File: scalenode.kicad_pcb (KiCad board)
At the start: 4 copper layers, 173.5 x 40 mm, 161 parts, among them IC2 TPS2378DDA, J1 QSE-020-01-F-D, J2 QSE-020-01-F-D, J3 1-2199230-6, J4 1140084168, J5 0473460001, J6 SS-74800-144, J7 DF40HC(3.0)-100DS-0.4v, J8 DF40HC(3.0)-100DS-0.4v, M1 compute-module-4-1.5mm, Q1 MMBT3906,215, Q2 MMBT3906,215, Q3 SI7848BDP-T1-E3, Q4 SI7450DP-T1-GE3, Q5 MMBT3906,215, T1 P0926NL, T2 POE300F-50L, U1 TS3USB30EDGSR, U2 TPS62823DLCT, U3 UCC3809D2, U4 TCMT1107

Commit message: Update designators
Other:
- board text added: "Expansion"
- board text added: "Video"
- board text removed: "Adapter Connector"
- board text removed: "Debug Connector"

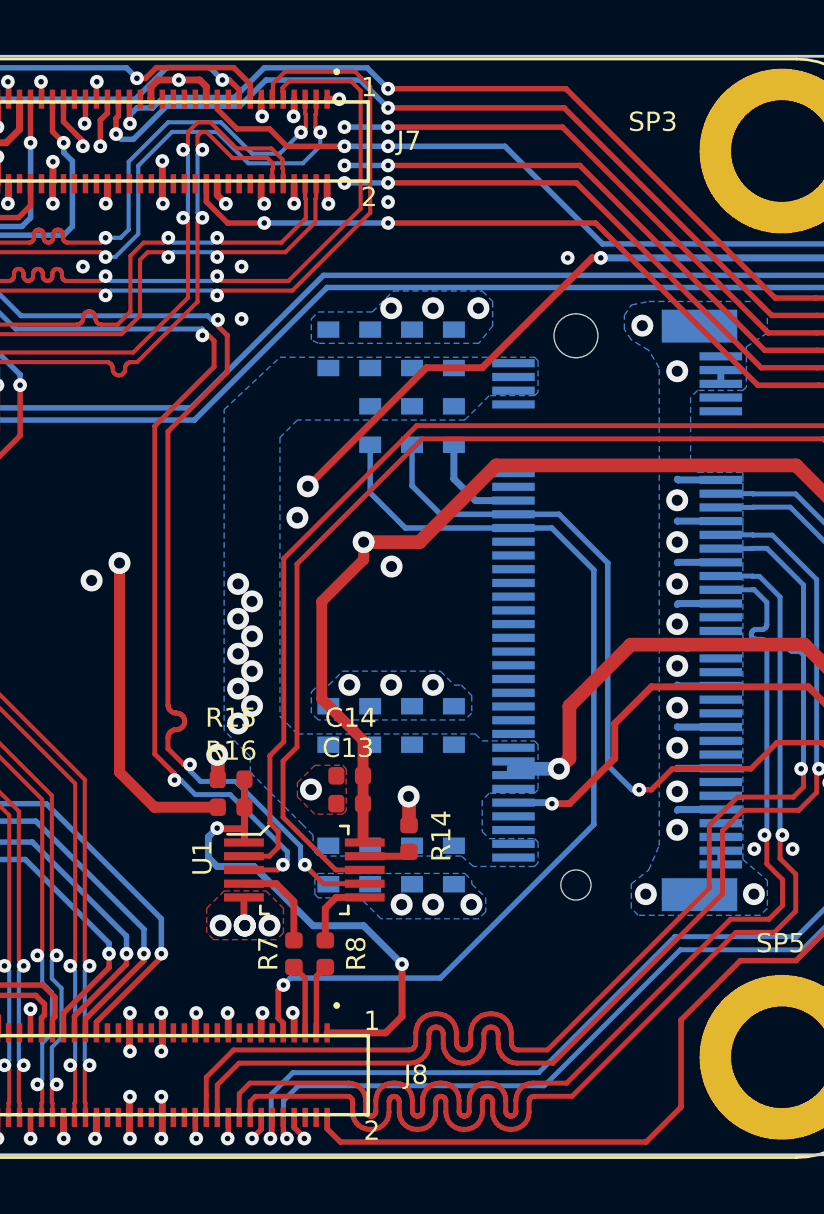
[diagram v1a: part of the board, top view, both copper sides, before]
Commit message: Fix J7 J8 footprints
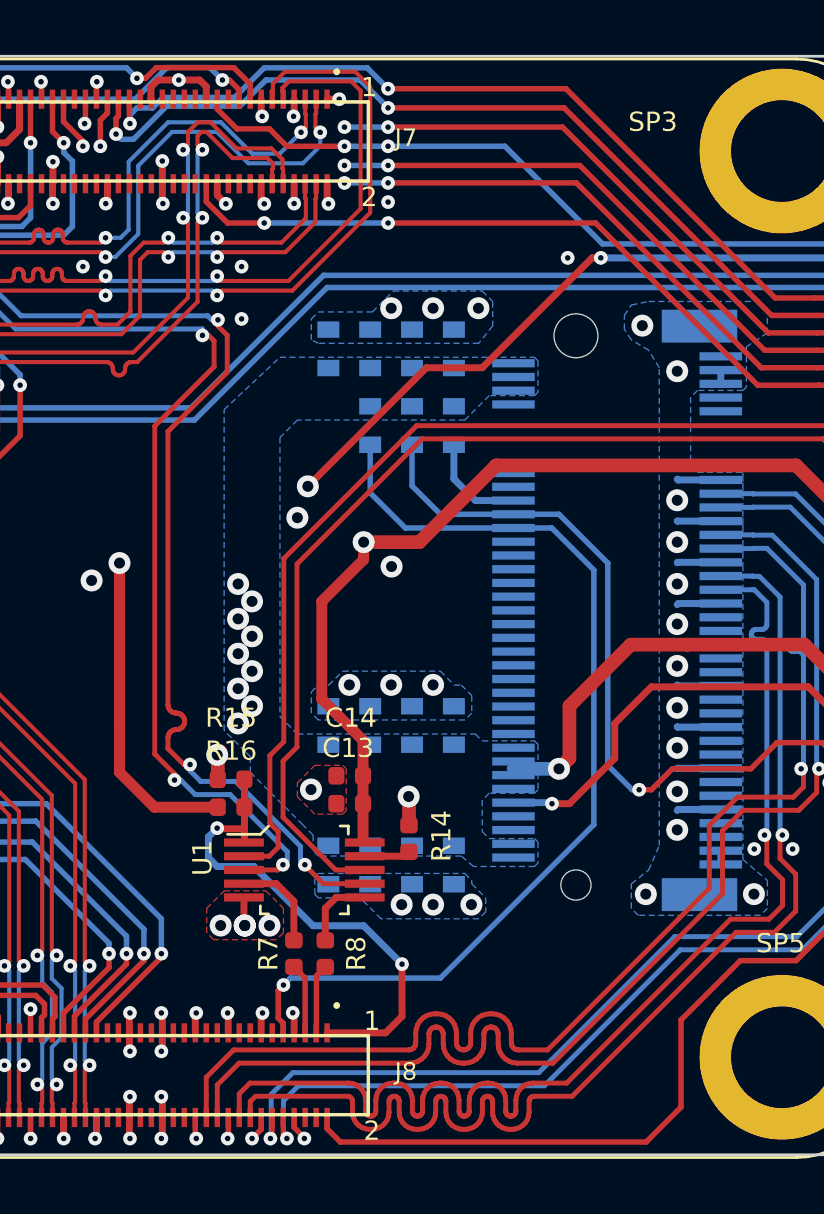
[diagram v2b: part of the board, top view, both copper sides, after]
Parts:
- J7, J8: footprint antmicro-footprints:DF40HC(3.0)-100DS-0.4v -> scalenode-footprints:DF40HC-3.0-100DS-0.4v

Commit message: Fix logotype
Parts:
- N1: footprint antmicro-footprints:antmicro-logo_scaled_15mm -> scalenode-footprints:antmicro-logo_scaled_15mm

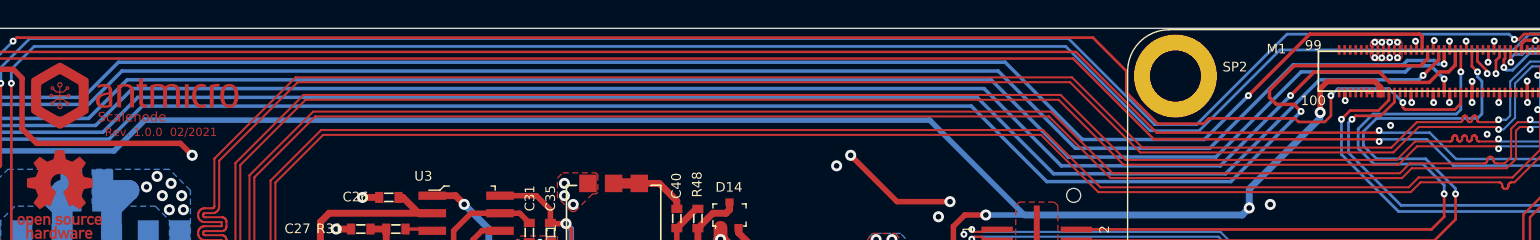
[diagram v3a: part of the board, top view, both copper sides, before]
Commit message: Connect GPIO_VREF signal to 3.3V_RPi
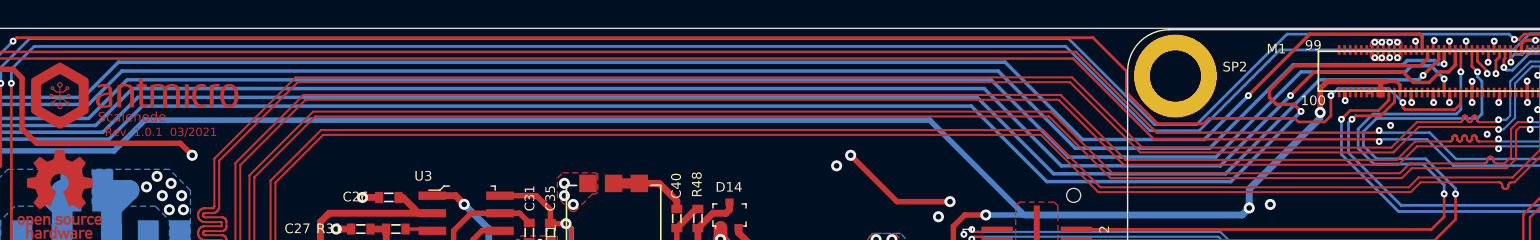
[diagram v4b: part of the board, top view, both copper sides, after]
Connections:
- J7 pad 78: GPIO_VREF -> 3V3_RPi
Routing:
- net 3V3_RPi: track 274.7 -> 277.0 mm
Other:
- board text added: "Rev. 1.0.1 03/2021"

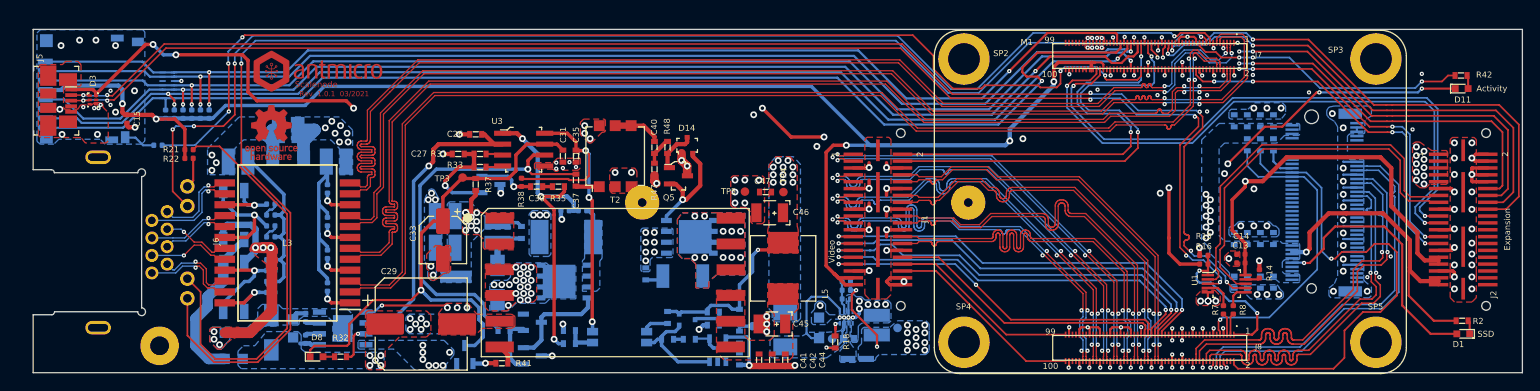
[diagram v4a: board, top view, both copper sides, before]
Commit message: Migration to KiCad 6
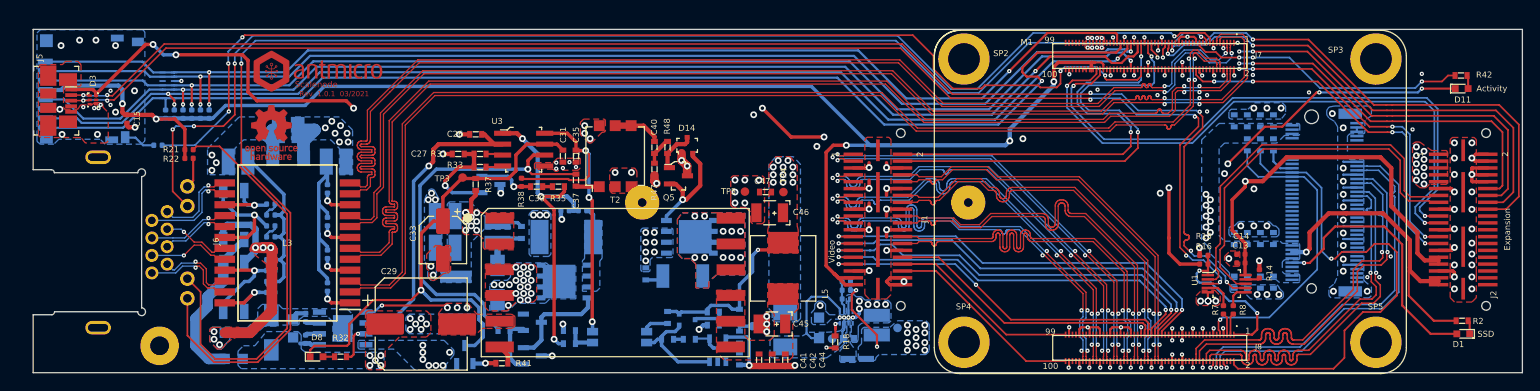
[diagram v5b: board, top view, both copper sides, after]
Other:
- outline, holes or cut-outs redrawn
- net class Default removed
- net class Diff_100 removed
- net class Diff_90 removed

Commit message: Implemented changes from rev 1.0.4. New components initial placement
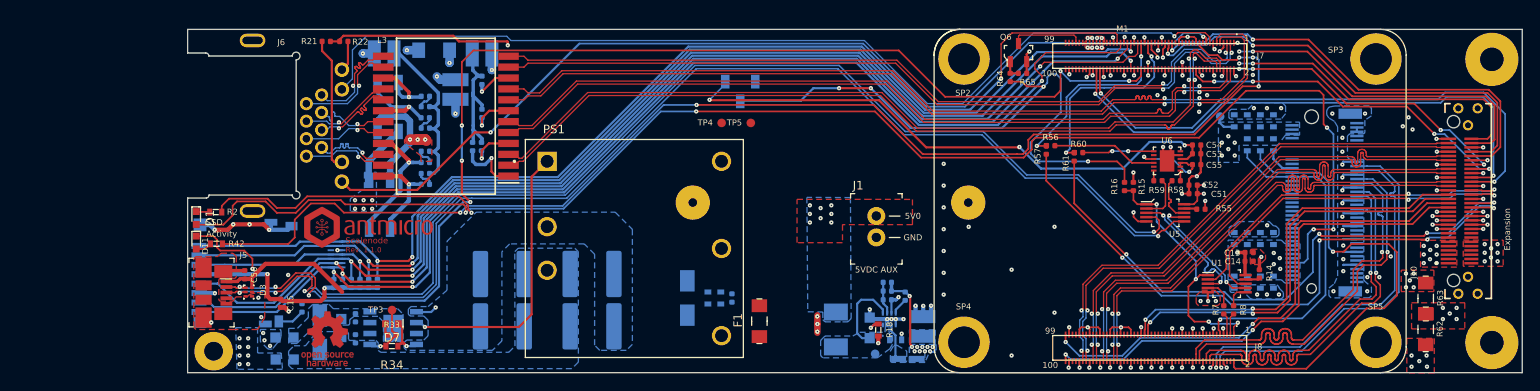
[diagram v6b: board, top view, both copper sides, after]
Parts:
- removed C21, C23, C24: C_10n_0402, scalenode-footprints:0402-cap
- removed C22: C_1n_1210_2kV, scalenode-footprints:1210-cap
- removed C38: C_100p_0402, scalenode-footprints:0402-cap
- removed C39: C_82n_0603, scalenode-footprints:0603-cap
- removed C40: C_470n_0603, scalenode-footprints:0603-cap
- removed C41, C42, C44: C_47u_0603, scalenode-footprints:0603-cap
- removed C43, C47: C_1u_0603, scalenode-footprints:0603-cap
- removed C45, C46: C_220u_KEMET_B, scalenode-footprints:KEMET_B
- removed C48: C_1n_0603, scalenode-footprints:0603-cap
- removed C49: C_1n2_0603, scalenode-footprints:0603-res
- removed D10: MURA120T3G, scalenode-footprints:DO-214AC
- removed D12: TLV431ACDBVR, scalenode-footprints:SOT-23-5
- removed D13, D14: BAV99W,115, scalenode-footprints:SOT-323
- removed D9: BAS16E6327HTSA1, scalenode-footprints:SOT-23-3
- removed IC2: TPS2378DDA, scalenode-footprints:SOIC127P600X170-9N
- removed J2: QSE-020-01-F-D, scalenode-footprints:QSE-020-01-XXX-D-A
- removed L4: DO1608C-332MLB, scalenode-footprints:L_6.3x4.5
- removed L5: DR74-R33-R, scalenode-footprints:L_DR74
- removed Q1, Q2, Q5: MMBT3906,215, scalenode-footprints:SOT-23-3
- removed Q3: SI7848BDP-T1-E3, scalenode-footprints:PowerPAK_SO-8_Single
- removed Q4: SI7450DP-T1-GE3, scalenode-footprints:PowerPAK_SO-8_Single
- removed R36: R_24k9_0402, scalenode-footprints:0402-res
- removed R37: R_30k1_0603, scalenode-footprints:0603-res
- removed R38: R_4k99_0402, scalenode-footprints:0402-res
- removed R39: R_24R9_0603, scalenode-footprints:0603-res
- removed R40: R_15k_0603, scalenode-footprints:0603-res
- removed R41: R_20R_0603, scalenode-footprints:0603-res
- removed R43: R_R33_2512, scalenode-footprints:2512
- removed R44: R_1k_0402, scalenode-footprints:0402-res
- removed R45, R46: R_1k_0603, scalenode-footprints:0603-res
- removed R47, R49: R_10k_0603, scalenode-footprints:0603-res
- removed R48, R53: R_49R9_0603, scalenode-footprints:0603-res
- removed R50: R_10R_2010, scalenode-footprints:2010-res
- removed R51, R54: R_41k2_0603, scalenode-footprints:0603-res
- removed R52: R_13k3_0603, scalenode-footprints:0603-res
- removed T1: P0926NL, scalenode-footprints:Pulse_P0926NL
- removed T2: POE300F-50L, scalenode-footprints:POE300F-24LD
- removed TP6: TP_SMD1MM, scalenode-footprints:Testpoint_smd_1mm
- removed U3: UCC3809D2, scalenode-footprints:SOIC-8_W3.9mm
- removed U4: TCMT1107, scalenode-footprints:TCMT1107
- added C51: C_100n_0402, scalenode-footprints:0402-cap, F.Cu at (172.2, 75.7)
- added C52: C_1u_0402, scalenode-footprints:0402-cap, F.Cu at (172.2, 74.8)
- added C53: C_1u_0402, scalenode-footprints:0402-cap, F.Cu at (172.6, 71.1)
- added C54: C_100n_0402, scalenode-footprints:0402-cap, F.Cu at (172.6, 70.1)
- added C55: C_100n_0402, scalenode-footprints:0402-cap, F.Cu at (172.6, 72.4)
- added C56: C_100n_0402, scalenode-footprints:0402-cap, F.Cu at (61.7, 85.2)
- added F1: 1206L450SLWR, antmicro-footprints:1206-res, F.Cu at (121.7, 90.6)
- added IC1: TPS2378DDA, scalenode-footprints:SOIC127P600X170-9N, B.Cu at (79.0, 91.4)
- added J10: LSHM-130-01-L-RH-A-S-K-TR, scalenode-footprints:SAMTEC_LSHM-130-01-XXX-RH-A-S-K-XX, F.Cu at (202.6, 76.6)
- added MP2: PCB_Mount_Hole_2.5_6.2, scalenode-footprints:Mount-hole-M2.5, F.Cu at (207.0, 93.1)
- added MP3: PCB_Mount_Hole_2.5_6.2, scalenode-footprints:Mount-hole-M2.5, F.Cu at (207.0, 60.1)
- added PS1: PDQE30-Q48-S5-D, antmicro-footprints:PDQE30-Q48, F.Cu at (107.1, 82.1)
- added Q6: BSS138-7-F, scalenode-footprints:SOT-23-3, F.Cu at (151.9, 59.3)
- added R55: R_10k_0402, scalenode-footprints:0402-res, F.Cu at (173.1, 77.6)
- added R56: R_220R_0402, scalenode-footprints:0402-res, F.Cu at (155.6, 70.2)
- added R57: R_220R_0402, scalenode-footprints:0402-res, F.Cu at (155.1, 70.7)
- added R58: R_22R_0402, scalenode-footprints:0402-res, F.Cu at (170.3, 74.2)
- added R59: R_22R_0402, scalenode-footprints:0402-res, F.Cu at (168.1, 74.2)
- added R60: R_220R_0402, scalenode-footprints:0402-res, F.Cu at (158.9, 71.0)
- added R61: R_220R_0402, scalenode-footprints:0402-res, F.Cu at (158.4, 71.5)
- added R62: R_0R_1206, scalenode-footprints:1206-res, F.Cu at (199.3, 91.6)
- added R63: R_0R_1206, scalenode-footprints:1206-res, F.Cu at (199.3, 88.0)
- added R64: R_470R_0402, scalenode-footprints:0402-res, F.Cu at (150.9, 62.2)
- added R65: R_10k_0402, scalenode-footprints:0402-res, F.Cu at (152.4, 61.7)
- added S1: CAS-120TA, scalenode-footprints:Switch_Slide_CAS-120TA, B.Cu at (119.5, 63.8)
- added U5: TS3USB30EDGSR, scalenode-footprints:MSOP-10_W3mm, F.Cu at (169.0, 78.0)
- added U6: FT234XD-R, scalenode-footprints:DFN-12-1EP_3x3mm, F.Cu at (169.2, 71.9)
- C20: value C_10n_0402 -> C_100n_0805_100V; footprint scalenode-footprints:0402-cap -> scalenode-footprints:0805-cap
- C26: value C_10n_0603 -> C_22u_2220_100V; footprint scalenode-footprints:0603-cap -> antmicro-footprints:2220-cap; moved to B.Cu
- C27: value C_270p_0603 -> C_10n_0402; footprint scalenode-footprints:0603-cap -> scalenode-footprints:0402-cap; moved to B.Cu
- C28: value C_100n_0805_100V -> C_22u_2220_100V; footprint scalenode-footprints:0805-cap -> antmicro-footprints:2220-cap
- C29: value C_47u_ELEC_100V -> C_22u_2220_100V; footprint scalenode-footprints:CP_Elec_10x10.5 -> antmicro-footprints:2220-cap; moved to B.Cu
- C30: value C_100n_0603 -> C_10n_0402; footprint scalenode-footprints:0603-cap -> scalenode-footprints:0402-cap; moved to B.Cu
- C31: value C_220n_0603_25V -> C_1n_1210_2kV; footprint scalenode-footprints:0603-cap -> scalenode-footprints:1210-cap; moved to B.Cu
- C32: value C_1u_1210_100V -> C_22u_2220_100V; footprint scalenode-footprints:1210-cap -> antmicro-footprints:2220-cap
- C33: value C_22u_ELEC_25V -> C_10n_0402; footprint scalenode-footprints:CP_Elec_5x5.8 -> scalenode-footprints:0402-cap; moved to B.Cu
- C34: value C_1u_1210_100V -> C_10n_0402; footprint scalenode-footprints:1210-cap -> scalenode-footprints:0402-cap
- C35: value C_1u_0603 -> C_47u_0603; moved to B.Cu
- C36: value C_1u_1210_100V -> C_47u_0603; footprint scalenode-footprints:1210-cap -> scalenode-footprints:0603-cap
- C37: value C_470n_0603 -> C_100n_0402; footprint scalenode-footprints:0603-cap -> scalenode-footprints:0402-cap; moved to B.Cu
- D1, D11: value KP-1608CGCK -> 598-8D80-107F; footprint scalenode-footprints:LED_0603 -> scalenode-footprints:LED_0603_R
- D7: value BAS16E6327HTSA1 -> KP-1608CGCK; footprint scalenode-footprints:SOT-23-3 -> scalenode-footprints:LED_0603; moved to F.Cu
- D8: value KP-1608CGCK -> SMAJ6.5A; footprint scalenode-footprints:LED_0603 -> antmicro-footprints:DO-214AC; moved to B.Cu
- J1: value QSE-020-01-F-D -> B2B-XH-A_LF__SN_; footprint scalenode-footprints:QSE-020-01-XXX-D-A -> antmicro-footprints:PinHeader_1x2_P2.5mm_Drill1.1mm
- R16: value R_2k2_0402 -> R_1k1_0402
- R23: value R_75R_0402 -> R_63R4_0402
- R24: value R_75R_0402 -> R_24k9_0402
- R31: value R_10k7_0603 -> R_75R_0402; footprint scalenode-footprints:0603-res -> scalenode-footprints:0402-res; moved to B.Cu
- R32: value R_10k_0603 -> R_75R_0402; footprint scalenode-footprints:0603-res -> scalenode-footprints:0402-res; moved to B.Cu
- R33: value R_4k64_0603 -> R_24k9_0402; footprint scalenode-footprints:0603-res -> scalenode-footprints:0402-res
- R34: value R_63R4_0402 -> R_15k_0603; footprint scalenode-footprints:0402-res -> scalenode-footprints:0603-res; moved to F.Cu
- R35: value R_10k_0603 -> R_0R_0402; footprint scalenode-footprints:0603-res -> antmicro-footprints:0402-res; moved to B.Cu
- moved D11 148.5 mm to (56.1, 81.4), turned to -90 degrees
- moved D1 148.2 mm to (56.1, 78.6), turned to -90 degrees
- moved R42 146.3 mm to (58.4, 81.6), turned to 180 degrees
- moved R2 145.8 mm to (58.4, 77.9), turned to 0 degrees
- moved TP2 44.9 mm to (175.4, 66.8)
- moved D8 43.7 mm to (113.3, 87.9), turned to 90 degrees
- moved R35 42.4 mm to (138.7, 87.7), turned to 90 degrees
- moved R32 30.8 mm to (82.8, 65.6)
- moved D3 28.8 mm to (62.2, 87.2)
- moved J5 28.8 mm to (56.9, 87.3)
- moved J4 27.9 mm to (61.7, 85.0)
- moved C15 27.9 mm to (65.9, 88.5)
- moved R13 27.8 mm to (77.2, 86.2)
- moved R5 27.8 mm to (72.1, 86.2)
- moved D2 27.8 mm to (72.4, 82.8)
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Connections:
- C20 pad 1: /PoE/PAIR12 -> /PoE/VDD_POE_IN
- C20 pad 2: Net-(C20-Pad2) -> VSS
- C26 pad 1: /PoE/CDB -> /PoE/VDD_POE_IN
- C27 pad 1: Net-(C27-Pad1) -> /PoE/PAIR12
- C27 pad 2: GNDD -> Net-(C27-Pad2)
- C28 pad 1: VDD -> /PoE/VDD_POE_IN
- C28 pad 2: VSS -> GNDD
- C29 pad 1: VDD -> /PoE/VDD_POE_IN
- C30 pad 1: Net-(C30-Pad1) -> /PoE/PAIR36
- C31 pad 1: /PoE/CTRL_VDD -> Net-(C31-Pad1)
- C31 pad 2: GNDD -> Earth
- C32 pad 1: Net-(C32-Pad1) -> /PoE/VDD_POE_IN
- C33 pad 1: /PoE/CTRL_VDD -> /PoE/PAIR45
- C33 pad 2: GNDD -> Net-(C33-Pad2)
- C34 pad 1: Net-(C32-Pad1) -> /PoE/PAIR78
- C34 pad 2: GNDD -> Net-(C34-Pad2)
- C35 pad 1: /PoE/CTRL_REF -> Net-(C35-Pad1)
- C35 pad 2: GNDD -> GND
- C36 pad 1: Net-(C32-Pad1) -> Net-(C35-Pad1)
- C36 pad 2: Net-(C36-Pad2) -> GND
- C37 pad 1: Net-(C37-Pad1) -> Net-(C35-Pad1)
- C37 pad 2: /PoE/CTRL_OUT -> GND
- D3 pad 1: /Interfaces/RPi_USB_N -> /Interfaces/CONN_USB_N
- D3 pad 2: /Interfaces/RPi_USB_P -> /Interfaces/CONN_USB_P
- D3 pad 3: Net-(D3-Pad3) -> unconnected-(D3-Pad3)
- D3 pad 5: Net-(D3-Pad5) -> unconnected-(D3-Pad5)
- D6 pad K: VDD -> /PoE/VDD_POE_IN
- D7 pad 2: (no net) -> GNDD
- FB2 pad 2: VDD -> /PoE/VDD_POE_IN
- J1 pad 1: HDMI0_D2_P -> VCC5V0
- J1 pad 2: GPIO14 -> GND
- J3 pad 11: Net-(J3-Pad11) -> unconnected-(J3-Pad11)
- J3 pad 13: Net-(J3-Pad13) -> unconnected-(J3-Pad13)
- J3 pad 17: Net-(J3-Pad17) -> unconnected-(J3-Pad17)
- J3 pad 19: Net-(J3-Pad19) -> unconnected-(J3-Pad19)
- J3 pad 20: Net-(J3-Pad20) -> unconnected-(J3-Pad20)
- J3 pad 22: Net-(J3-Pad22) -> unconnected-(J3-Pad22)
- J3 pad 23: Net-(J3-Pad23) -> unconnected-(J3-Pad23)
- J3 pad 24: Net-(J3-Pad24) -> unconnected-(J3-Pad24)
- J3 pad 25: Net-(J3-Pad25) -> unconnected-(J3-Pad25)
- J3 pad 26: Net-(J3-Pad26) -> unconnected-(J3-Pad26)
- J3 pad 28: Net-(J3-Pad28) -> unconnected-(J3-Pad28)
- J3 pad 29: Net-(J3-Pad29) -> unconnected-(J3-Pad29)
- J3 pad 30: Net-(J3-Pad30) -> unconnected-(J3-Pad30)
- J3 pad 31: Net-(J3-Pad31) -> unconnected-(J3-Pad31)
- J3 pad 32: Net-(J3-Pad32) -> unconnected-(J3-Pad32)
- J3 pad 34: Net-(J3-Pad34) -> unconnected-(J3-Pad34)
- J3 pad 35: Net-(J3-Pad35) -> unconnected-(J3-Pad35)
- J3 pad 36: Net-(J3-Pad36) -> unconnected-(J3-Pad36)
- J3 pad 37: Net-(J3-Pad37) -> unconnected-(J3-Pad37)
- J3 pad 38: Net-(J3-Pad38) -> unconnected-(J3-Pad38)
- J3 pad 40: Net-(J3-Pad40) -> unconnected-(J3-Pad40)
- J3 pad 42: Net-(J3-Pad42) -> unconnected-(J3-Pad42)
- J3 pad 44: Net-(J3-Pad44) -> unconnected-(J3-Pad44)
- J3 pad 46: Net-(J3-Pad46) -> unconnected-(J3-Pad46)
- J3 pad 48: Net-(J3-Pad48) -> unconnected-(J3-Pad48)
- J3 pad 5: Net-(J3-Pad5) -> unconnected-(J3-Pad5)
- J3 pad 56: Net-(J3-Pad56) -> unconnected-(J3-Pad56)
- J3 pad 58: Net-(J3-Pad58) -> unconnected-(J3-Pad58)
- J3 pad 6: Net-(J3-Pad6) -> unconnected-(J3-Pad6)
- J3 pad 67: Net-(J3-Pad67) -> unconnected-(J3-Pad67)
- J3 pad 68: Net-(J3-Pad68) -> unconnected-(J3-Pad68)
- J3 pad 69: Net-(J3-Pad69) -> unconnected-(J3-Pad69)
- J3 pad 7: Net-(J3-Pad7) -> unconnected-(J3-Pad7)
- J3 pad 8: Net-(J3-Pad8) -> unconnected-(J3-Pad8)
- J4 pad ~: GND -> (no net)
- J5 pad 2: /Interfaces/RPi_USB_N -> /Interfaces/CONN_USB_N
- J5 pad 3: /Interfaces/RPi_USB_P -> /Interfaces/CONN_USB_P
- J5 pad 4: Net-(J5-Pad4) -> unconnected-(J5-Pad4)
- J7 pad 19: Net-(J7-Pad19) -> unconnected-(J7-Pad19)
- J7 pad 51: GPIO15 -> RPi_RXD
- J7 pad 55: GPIO14 -> RPi_TXD
- J7 pad 64: Net-(J7-Pad64) -> unconnected-(J7-Pad64)
- J7 pad 68: Net-(J7-Pad68) -> unconnected-(J7-Pad68)
- J7 pad 70: Net-(J7-Pad70) -> unconnected-(J7-Pad70)
- J7 pad 72: Net-(J7-Pad72) -> unconnected-(J7-Pad72)
- J7 pad 73: Net-(J7-Pad73) -> unconnected-(J7-Pad73)
- J7 pad 93: nRPIBOOT -> /Compute module/nRPi_BOOT
- J8 pad 4: Net-(J8-Pad4) -> unconnected-(J8-Pad4)
- J8 pad 6: Net-(J8-Pad6) -> unconnected-(J8-Pad6)
- R16 pad 1: /Interfaces/VBus_Slave -> USBOTG_ID
- R16 pad 2: USBOTG_ID -> PROG_MODE
- R23 pad 1: Net-(C20-Pad2) -> Net-(IC1-Pad3)
- R23 pad 2: Net-(C22-Pad1) -> VSS
- R24 pad 1: Net-(C21-Pad2) -> /PoE/VDD_POE_IN
- R24 pad 2: Net-(C22-Pad1) -> Net-(IC1-Pad2)
- R25 pad 1: Net-(C23-Pad2) -> Net-(C27-Pad2)
- R25 pad 2: Net-(C22-Pad1) -> Net-(C31-Pad1)
- R26 pad 1: Net-(C24-Pad2) -> Net-(C30-Pad2)
- R26 pad 2: Net-(C22-Pad1) -> Net-(C31-Pad1)
- R31 pad 1: Net-(R31-Pad1) -> Net-(C33-Pad2)
- R31 pad 2: Net-(C27-Pad1) -> Net-(C31-Pad1)
- R32 pad 1: Net-(D8-Pad2) -> Net-(C34-Pad2)
- R32 pad 2: Net-(IC2-Pad7) -> Net-(C31-Pad1)
- R33 pad 1: Net-(R33-Pad1) -> Net-(D7-Pad1)
- R33 pad 2: Net-(C27-Pad1) -> /PoE/VDD_POE_IN
- R34 pad 1: Net-(IC2-Pad3) -> GNDD
- R34 pad 2: VSS -> /PoE/VDD_POE_IN
- R35 pad 1: /PoE/CTRL_FB -> Net-(R35-Pad1)
- R35 pad 2: Net-(C30-Pad2) -> 3V3_SSD
- SP1 pad 1: Net-(SP1-Pad1) -> unconnected-(SP1-Pad1)
- SP2 pad 1: Net-(SP2-Pad1) -> unconnected-(SP2-Pad1)
- SP3 pad 1: Net-(SP3-Pad1) -> unconnected-(SP3-Pad1)
- SP4 pad 1: Net-(SP4-Pad1) -> unconnected-(SP4-Pad1)
- SP5 pad 1: Net-(SP5-Pad1) -> unconnected-(SP5-Pad1)
- SP6 pad 1: Net-(SP6-Pad1) -> unconnected-(SP6-Pad1)
- TP3 pad 1: /PoE/CTRL_VDD -> /PoE/VDD_POE_IN
- TP4 pad 1: VCC5V0 -> GND
- TP5 pad 1: GND -> VCC5V0
- U1 pad 2: Arty_USB_P -> Adapter_USB_P
- U1 pad 8: Arty_USB_N -> Adapter_USB_N
- U2 pad 4: (no net) -> Net-(R35-Pad1)
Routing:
- net 3V3_RPi: track 277.0 -> 74.3 mm, vias 9 -> 16
- net /Interfaces/RPi_USB_N: track 165.6 -> 15.1 mm, vias 6 -> 2
- net /Interfaces/RPi_USB_P: track 163.2 -> 15.7 mm, vias 6 -> 2
- net /Interfaces/CONN_USB_N: track 0.00 -> 142.0 mm, vias 0 -> 4
- net /Interfaces/CONN_USB_P: track 0.00 -> 140.5 mm, vias 0 -> 4
- net Net-(D1-Pad2): track 31.1 -> 170.9 mm, vias 1 -> 5
- net Net-(J7-Pad21): track 32.8 -> 147.1 mm, vias 3 -> 5
- net Adapter_RXD: track 0.00 -> 72.4 mm, vias 0 -> 4
- net PROG_MODE: track 0.00 -> 70.7 mm, vias 0 -> 4
- net /Interfaces/VBus_Slave: track 152.7 -> 83.5 mm, vias 6 -> 3
- net Adapter_TXD: track 0.00 -> 68.4 mm, vias 0 -> 4
- net /PoE/CTRL_VDD: track 62.2 -> 0.00 mm, vias 1 -> 0
- net ETH_LEDY: track 172.8 -> 115.7 mm
- net GPIO15: track 53.3 -> 0.00 mm, vias 2 -> 0
- net GPIO14: track 50.3 -> 0.00 mm, vias 2 -> 0
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- added copper zone on B.Cu, net /PoE/VDD_POE_IN
- added copper zone on F.Cu, net 3V3_OUT
- added copper zone on In2.Cu, net 3V3_OUT
- added copper zone on F.Cu, net 3V3_RPi
- added copper zone on In2.Cu, net 3V3_RPi
- added copper zone on F.Cu, net 3V3_SSD
- added copper zone on B.Cu, net Net-(D4-Pad1)
- added copper zone on In2.Cu, net Net-(D4-Pad1)
- added copper zone on In2.Cu, net Net-(D4-Pad2)
- removed copper zone on B.Cu, net Earth
- removed copper zone on In2.Cu, net GND
- removed copper zone on F.Cu, net GNDD
- removed copper zone on In1.Cu, net GNDD
- removed copper zone on In2.Cu, net GNDD
- removed copper zone on B.Cu, net Net-(C32-Pad1)
- removed copper zone on F.Cu, net Net-(C32-Pad1)
- removed copper zone on F.Cu, net Net-(C41-Pad1)
- removed copper zone on B.Cu, net Net-(D10-PadA)
- removed copper zone on F.Cu, net Net-(D10-PadA)
- removed copper zone on B.Cu, net Net-(Q3-Pad5)
- removed copper zone on F.Cu, net Net-(Q3-Pad5)
- removed copper zone on B.Cu, net Net-(Q4-Pad1)
- removed copper zone on B.Cu, net VDD
- removed copper zone on F.Cu, net VDD
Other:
- board size 173.5 x 40 mm -> 155.5 x 40 mm
- board text added: "0.018 mm"
- board text added: "0.02 mm"
- board text added: "0.035 mm"
- board text added: "0.12 mm"
- board text added: "1"
- board text added: "1.2 mm"
- board text added: "2"
- board text added: "3"
- board text added: "3.5"
- board text added: "4"
- board text added: "4.2"
- board text added: "5"
- board text added: "5V0"
- board text added: "5VDC AUX"
- board text added: "6"
- board text added: "7"
- board text added: "8"
- board text added: "9"
- board text added: "Bottom Layer"
- board text added: "Bottom Solder"
- board text added: "Constant"
- board text added: "Copper"
- board text added: "Dielectric 1"
- board text added: "Dielectric 2"
- board text added: "Dielectric 3"
- board text added: "FR-4"
- board text added: "GND"
- board text added: "Gold plating (ENIG, selective)"
- board text added: "Layer"
- board text added: "Material"
- board text added: "Name"
- board text added: "PROG"
- board text added: "Power Plane 1"
- board text added: "Power Plane 2"
- board text added: "Prepreg"
- board text added: "Recommended PCB finish:"
- board text added: "Recommended PCB stackup"
- board text added: "Rev. 1.1.0"
- board text added: "Silkscreen: white"
- board text added: "Solder Resist"
- board text added: "Solder mask: matt black"
- board text added: "Suggested prepreg material is ISOLA PR2116"
- board text added: "The design includes high speed signaling"
- board text added: "Thickness"
- board text added: "Top Layer"
- board text added: "Top Solder"
- board text removed: "Rev. 1.0.0 02/2021"
- board text removed: "Rev. 1.0.1 03/2021"
- board text removed: "Video"
